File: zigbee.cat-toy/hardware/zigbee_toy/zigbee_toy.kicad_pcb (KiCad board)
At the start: 2 copper layers, 40 x 26 mm, 60 parts, among them J1 USB-C 16P, J2 SWD, J3 LiPo 1S (JST-PH), J4 MOTOR, J5 SPEAKER, Q1 AO3401A, Q2 AO3400A, SW1 PAIR, U1 E73-2G4M08S1C, U2 DRV8213DSGR, U3 LIS2DH12TR, U4 TP4054-42-SOT25R, U5 XB5353A, Y1 32.768k 12.5pF

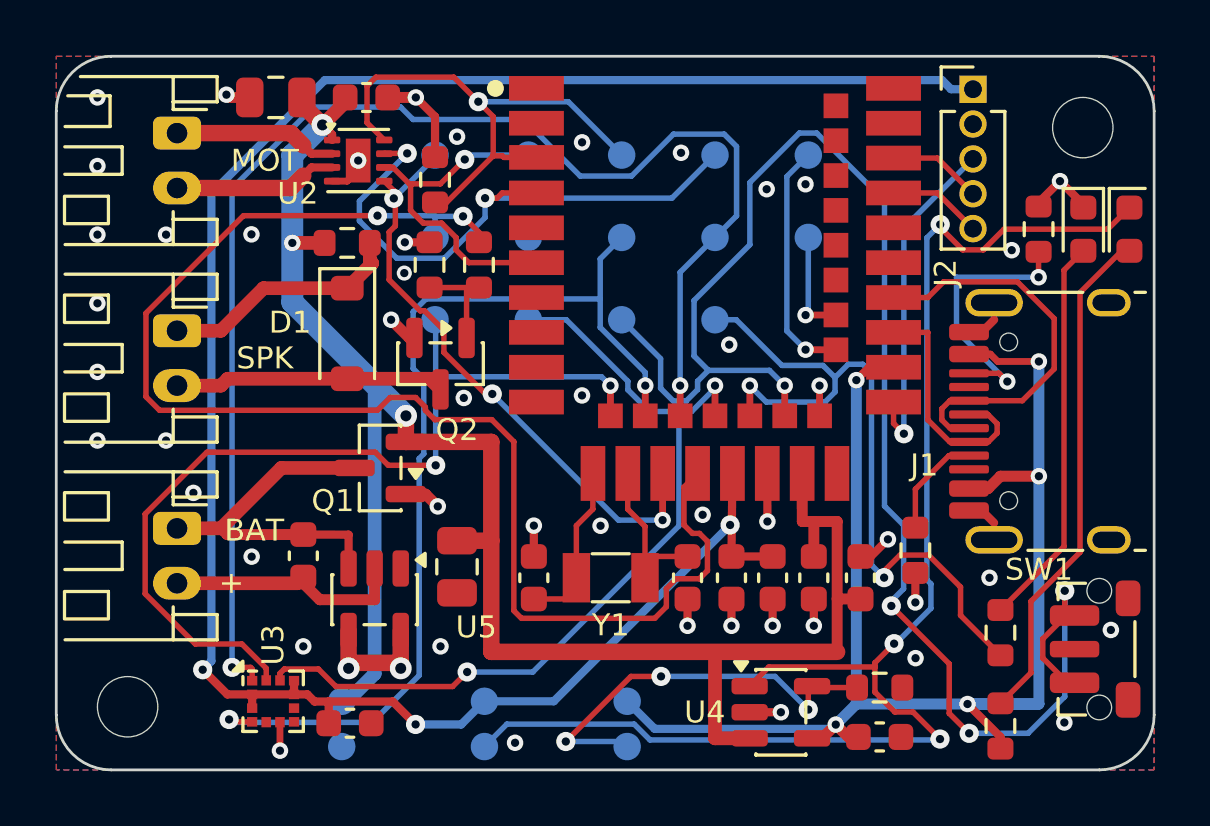
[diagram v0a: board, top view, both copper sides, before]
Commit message: zigbee.cat-toy: rev B board (ESP32-C6), JLC Economic PCBA
- ESP32-C6-MINI-1U-H4 replaces the nRF52840 E73; RT9080 3.3 V regulator,
  1M/1M battery divider, MSKSEMI LIS2DW12TR-MS accelerometer (not ST's),
  one red status LED. Every assembled part is Economic-eligible.
- Module 1 mm from the top edge (JLC Economic edge rule); antenna keepout
  so the PCB-antenna MINI-1 drops onto the same pads.
- Re-routed: USB pair under the module edge, nothing on F.Cu under the
  USB-C, no B.Cu under the crystal, 10 uF at the module 3V3 pin.
- Ball and pod checks cover a MINI-1 antenna overhang.
- README rewritten for rev B; rev A lives under the zigbee.cat-toy/rev-a tag.

Co-Authored-By: Claude Opus 5.5 <noreply@anthropic.com>
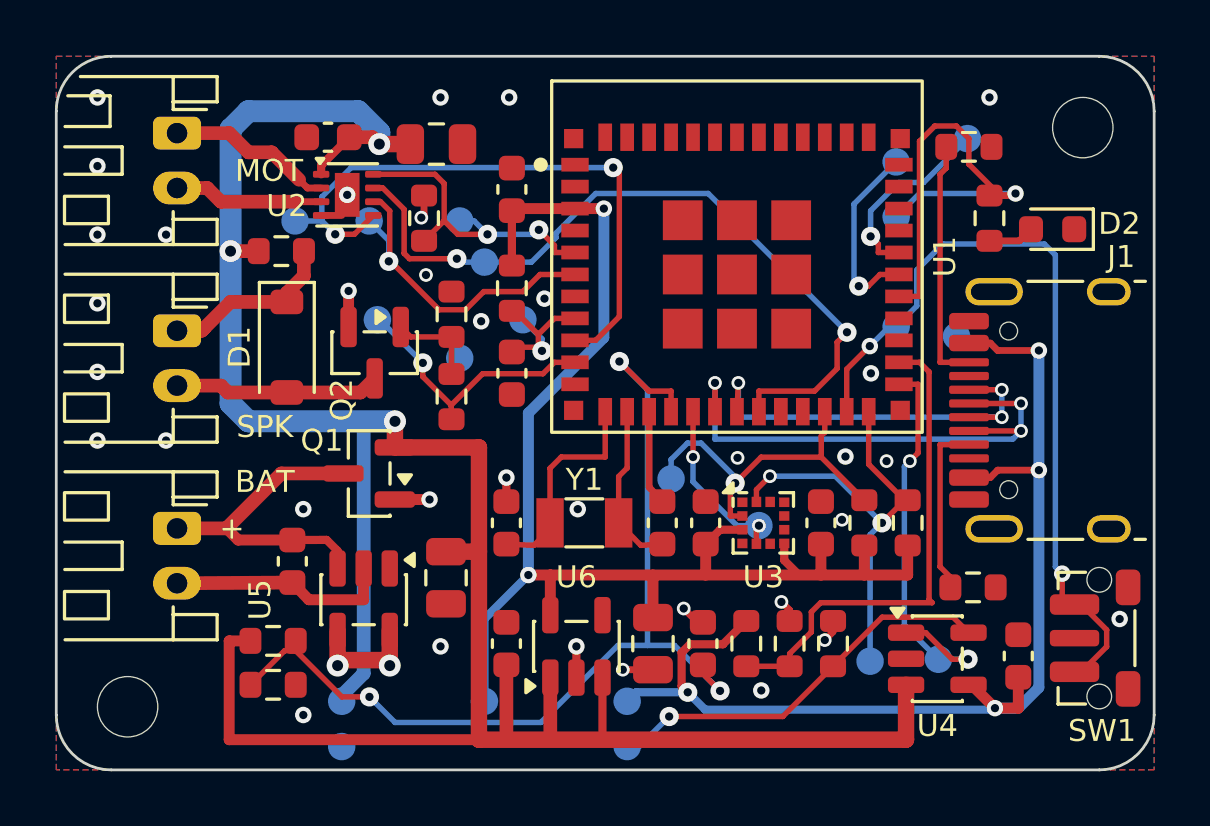
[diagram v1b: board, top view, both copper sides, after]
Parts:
- removed C7: 100n, Capacitor_SMD:C_0603_1608Metric
- removed D3: RED (status), LED_SMD:LED_0603_1608Metric
- removed J2: SWD, Connector_PinHeader_1.27mm:PinHeader_1x05_P1.27mm_Vertical
- removed R5: 1k, Resistor_SMD:R_0603_1608Metric
- removed TP14: INT2, TestPoint:TestPoint_Pad_D1.0mm
- added C11: 100n, Capacitor_SMD:C_0603_1608Metric, F.Cu at (23.7, 17.0)
- added C16: 100n, Capacitor_SMD:C_0603_1608Metric, F.Cu at (23.6, 21.4)
- added C5: 1u, Capacitor_SMD:C_0603_1608Metric, F.Cu at (16.6, 11.6)
- added R12: 1M, Resistor_SMD:R_0603_1608Metric, F.Cu at (7.90, 21.3)
- added R13: 1M, Resistor_SMD:R_0603_1608Metric, F.Cu at (7.90, 22.9)
- added R14: 68k, Resistor_SMD:R_0603_1608Metric, F.Cu at (25.1, 21.4)
- added R15: 100k, Resistor_SMD:R_0603_1608Metric, F.Cu at (26.7, 21.4)
- added R16: 4.7k, Resistor_SMD:R_0603_1608Metric, F.Cu at (29.4, 17.0)
- added R17: 4.7k, Resistor_SMD:R_0603_1608Metric, F.Cu at (31.0, 17.0)
- added R9: 10k, Resistor_SMD:R_0603_1608Metric, F.Cu at (16.6, 8.45)
- added TP21: EN, TestPoint:TestPoint_Pad_D1.0mm, B.Cu at (17.0, 9.60)
- added TP22: GND, TestPoint:TestPoint_Pad_D1.0mm, B.Cu at (32.8, 10.2)
- added U6: RT9080-33GJ5, Package_TO_SOT_SMD:TSOT-23-5, F.Cu at (18.9, 21.5)
- C8: value 4.7u -> 22u; footprint Capacitor_SMD:C_0603_1608Metric -> Capacitor_SMD:C_0805_2012Metric
- C9: value 100n -> 10u
- D2: value RED (charging) -> RED (status)
- SW1: value PAIR -> PAIR / BOOT
- TP17: value BTN -> BOOT
- TP2: value VDD -> 3V3
- U1: value E73-2G4M08S1C -> ESP32-C6-MINI-1U-H4; footprint zigbee_toy:Ebyte_E73-2G4M08S1C -> zigbee_toy:ESP32-C6-MINI-1U
- U3: value LIS2DH12TR -> LIS2DW12TR-MS
- moved U3 19.0 mm to (25.8, 17.0)
- moved C10 18.6 mm to (27.9, 17.0), turned to 90 degrees
- moved R4 18.5 mm to (34.0, 5.90), turned to -90 degrees
- moved TP5 16.8 mm to (32.1, 22.0)
- moved TP16 16.4 mm to (29.6, 22.0)
- moved C9 16.3 mm to (16.6, 4.85), turned to 90 degrees
- moved TP13 14.0 mm to (25.6, 17.1)
- moved C6 13.1 mm to (16.4, 21.4)
- moved TP17 10.0 mm to (30.6, 9.85)
- moved TP10 9.26 mm to (15.6, 7.50)
- moved TP15 8.98 mm to (22.4, 15.4)
- moved TP18 7.59 mm to (30.6, 5.85)
- moved TP9 6.37 mm to (14.7, 6.00)
- moved TP8 6.28 mm to (11.4, 6.00)
- moved C2 6.09 mm to (13.8, 3.20), turned to 0 degrees
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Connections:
- net XL2 renamed XTAL_N
- C10 pad 1: VDD -> 3V3
- C12 pad 1: XL1 -> XTAL_P
- C8 pad 1: VDD -> 3V3
- C9 pad 1: VDD -> 3V3
- D2 pad 1: CHG_STAT -> GND
- D2 pad 2: CHG_LED -> LED_A
- R4 pad 1: VBUS -> LED_STATUS
- R4 pad 2: CHG_LED -> LED_A
- TP2 pad 1: VDD -> 3V3
- U1 pad 1: (no net) -> GND
- U1 pad 10: (no net) -> SPK_PWM
- U1 pad 11: XL1 -> GND
- U1 pad 12: ACC_INT1 -> XTAL_P
- U1 pad 14: I2C_SDA -> GND
- U1 pad 15: MOT_PWM -> VBAT_SENSE
- U1 pad 16: I2C_SCL -> ACC_INT1
- U1 pad 17: SPK_PWM -> USB_DN
- U1 pad 18: ACC_INT2 -> USB_DP
- U1 pad 19: VDD -> MOT_GAINSEL
- U1 pad 2: (no net) -> GND
- U1 pad 20: LED_STATUS -> (no net)
- U1 pad 21: GND -> (no net)
- U1 pad 22: BTN -> I2C_SDA
- U1 pad 23: VBAT -> BTN
- U1 pad 24: GND -> I2C_SCL
- U1 pad 25: (no net) -> CHG_STAT
- U1 pad 26: nRESET -> VBUS_SENSE
- U1 pad 27: VBUS -> (no net)
- U1 pad 28: DBG_TX -> (no net)
- U1 pad 29: USB_DN -> LED_STATUS
- U1 pad 3: MOT_IPROPI -> 3V3
- U1 pad 31: USB_DP -> DBG_TX
- U1 pad 36: (no net) -> GND
- U1 pad 37: SWDIO -> GND
- U1 pad 38: (no net) -> GND
- U1 pad 39: SWCLK -> GND
- U1 pad 4: MOT_GAINSEL -> (no net)
- U1 pad 40: (no net) -> GND
- U1 pad 41: (no net) -> GND
- U1 pad 42: (no net) -> GND
- U1 pad 43: (no net) -> GND
- U1 pad 5: GND -> MOT_IPROPI
- U1 pad 8: (no net) -> EN
- U1 pad 9: (no net) -> MOT_PWM
- U3 pad 1: I2C_SCL -> (no net)
- U3 pad 10: VDD -> (no net)
- U3 pad 11: ACC_INT2 -> (no net)
- U3 pad 12: ACC_INT1 -> I2C_SCL
- U3 pad 2: VDD -> I2C_SDA
- U3 pad 3: VDD -> 3V3
- U3 pad 4: I2C_SDA -> (no net)
- U3 pad 5: GND -> ACC_INT1
- U3 pad 6: GND -> (no net)
- U3 pad 7: GND -> 3V3
- U3 pad 9: VDD -> GND
- Y1 pad 1: XL1 -> XTAL_P
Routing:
- net VDD: track 76.6 -> 0.00 mm, vias 3 -> 0
- net 3V3: track 0.00 -> 49.3 mm, vias 0 -> 2
- net SPK_PWM: track 51.2 -> 9.95 mm, vias 2 -> 1
- net CHG_STAT: track 51.3 -> 15.2 mm, vias 3 -> 2
- net VBAT_SENSE: track 0.00 -> 36.0 mm, vias 0 -> 3
- net I2C_SCL: track 50.8 -> 16.2 mm
- net ACC_INT2: track 31.6 -> 0.00 mm, vias 2 -> 0
- net BTN: track 57.9 -> 29.0 mm, vias 4 -> 2
- net ACC_INT1: track 33.5 -> 6.31 mm
- net I2C_SDA: track 36.5 -> 13.2 mm, vias 2 -> 1
- net VBAT: track 69.3 -> 92.5 mm
- net CHG_LED: track 18.6 -> 0.00 mm
- net VBUS_SENSE: track 0.00 -> 18.1 mm
- net GND: track 30.6 -> 17.3 mm, vias 50 -> 37
- net LED_A: track 14.3 -> 1.69 mm
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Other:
- board text added: "3V3"
- board text added: "BOOT"
- board text added: "EN"
- board text added: "rev B 2026-10"
- board text removed: "CHG"
- board text removed: "CLK"
- board text removed: "DIO"
- board text removed: "INT2"
- board text removed: "RST"
- board text removed: "VDD"
- board text removed: "rev A 2026-10"

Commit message: zigbee.cat-toy: rev B review fixes (driver ground loop, module vias, silk)
From an EE friend's review and the DRV8213 datasheet's layout section:
- C3 flipped so its ground pad drops straight onto the driver's thermal
  pad (return path 14.7 mm -> 1.2 mm); two thermal pad vias instead of one;
  ground via at C2 (18.7 mm -> 4.1 mm)
- IN2 rerouted on the back layer below the driver instead of under it, so
  the back plane under the driver is whole again; EN reshuffled to make room,
  TP21 sits on the EN via
- C2 10 uF -> 22 uF (same part as C1/C8)
- vias in 7 of the module's 9 centre ground pads (module ground to the
  driver 21 mm -> 6.5 mm)
- route generator chamfers 90-degree corners (29 -> 8, the rest inside pads
  or on vias)
- front refs all horizontal, one size; title and paw moved into the bare
  antenna keepout strip on the back
- MOT_DIR/MOT_PWM renamed MOT_IN1/MOT_IN2: PWM drive/brake on both pins
  (drive/coast loses IPROPI while coasting)

Co-Authored-By: Claude Opus 5.5 <noreply@anthropic.com>
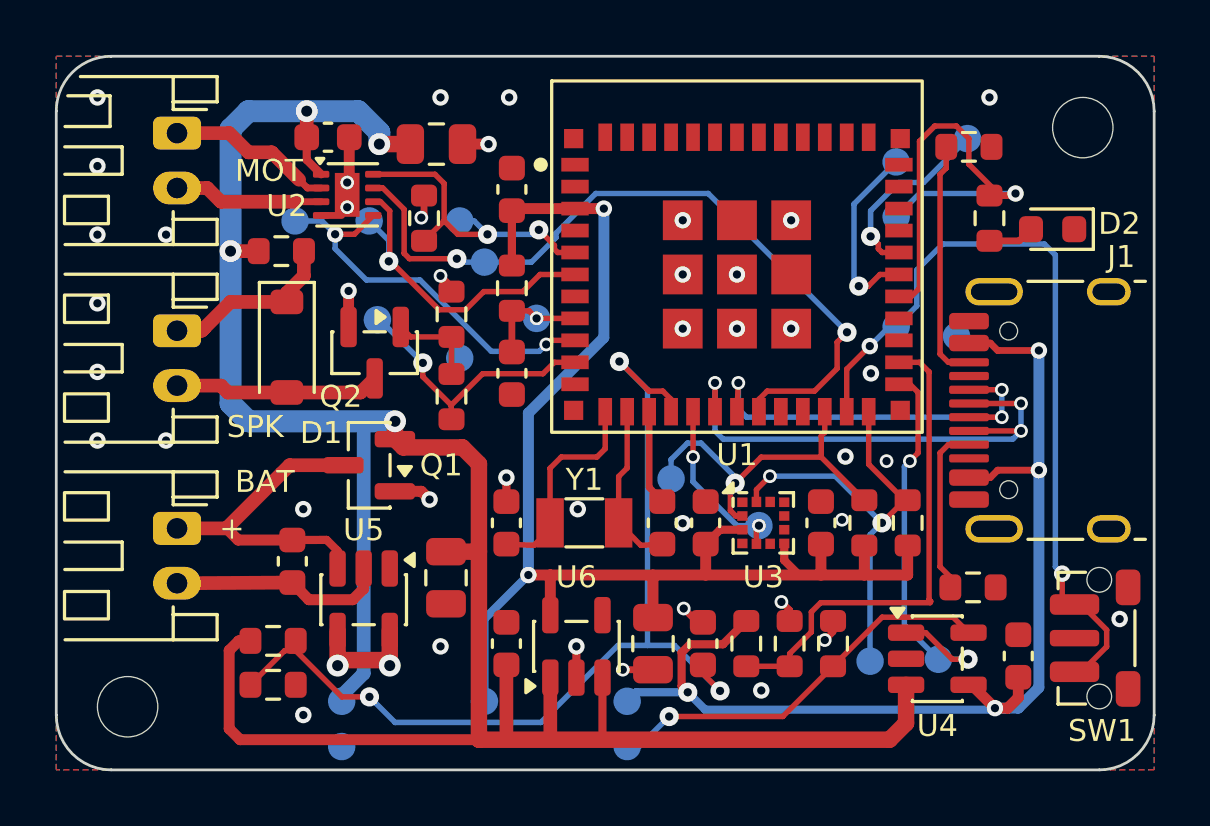
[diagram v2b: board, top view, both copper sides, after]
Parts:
- C2: value 10u 25V -> 22u
- TP7: value PWM -> IN2
- TP8: value DIR -> IN1
- moved TP21 0.50 mm to (17.5, 9.55)
- moved Q1 0.30 mm to (11.4, 14.9)
- turned C3 to 0 degrees
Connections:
- net MOT_DIR renamed MOT_IN1
- net MOT_PWM renamed MOT_IN2
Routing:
- net MOT_IN2: track 22.8 -> 14.3 mm
- net GND: track 17.3 -> 20.6 mm, vias 37 -> 44
- net EN: track 6.01 -> 3.91 mm
- net VBAT: track 92.5 -> 90.7 mm, vias 3 -> 4
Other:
- board text added: "IN1"
- board text added: "IN2"
- board text removed: "DIR"
- board text removed: "PWM"

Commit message: zigbee.cat-toy: rev B shrunk to 36 x 23 mm (was 40 x 26)
- 0402 Basic passives; bulk caps stay 0603/0805. VBUS divider 33k/51k
  (68k has no Basic 0402)
- motor and speaker on JST-SH (SMD, assembled); battery stays JST-PH
- USBLC6-2SC6 on D+/D-; 10 nF on IPROPI (DRV8213 datasheet 8.4.2.2)
- new floorplan and routing: power, driver loop, USB, BTN, the
  accelerometer block and ground vias by hand, the rest Freerouting
  (frozen); every ground pad has its own via or reaches the pour
- module pins 25/26 swapped: VBUS_SENSE on IO19, CHG_STAT on IO20
- the button's two pin-1 pads count as one terminal (KiCad jumper pads)
- gen_silk clips footprint outlines at pads and other parts' silk;
  check_spacing.py checks real body/pad gaps, courtyard overlap is a
  warning
- pod.py and ball.py read the board from placement.py; pod bay grows for
  the 103450 cell; ball board moves so the H2 standoff clears the motor.
  Both --check CLEAN against the new board STEP

Co-Authored-By: Claude Opus 5.5 <noreply@anthropic.com>
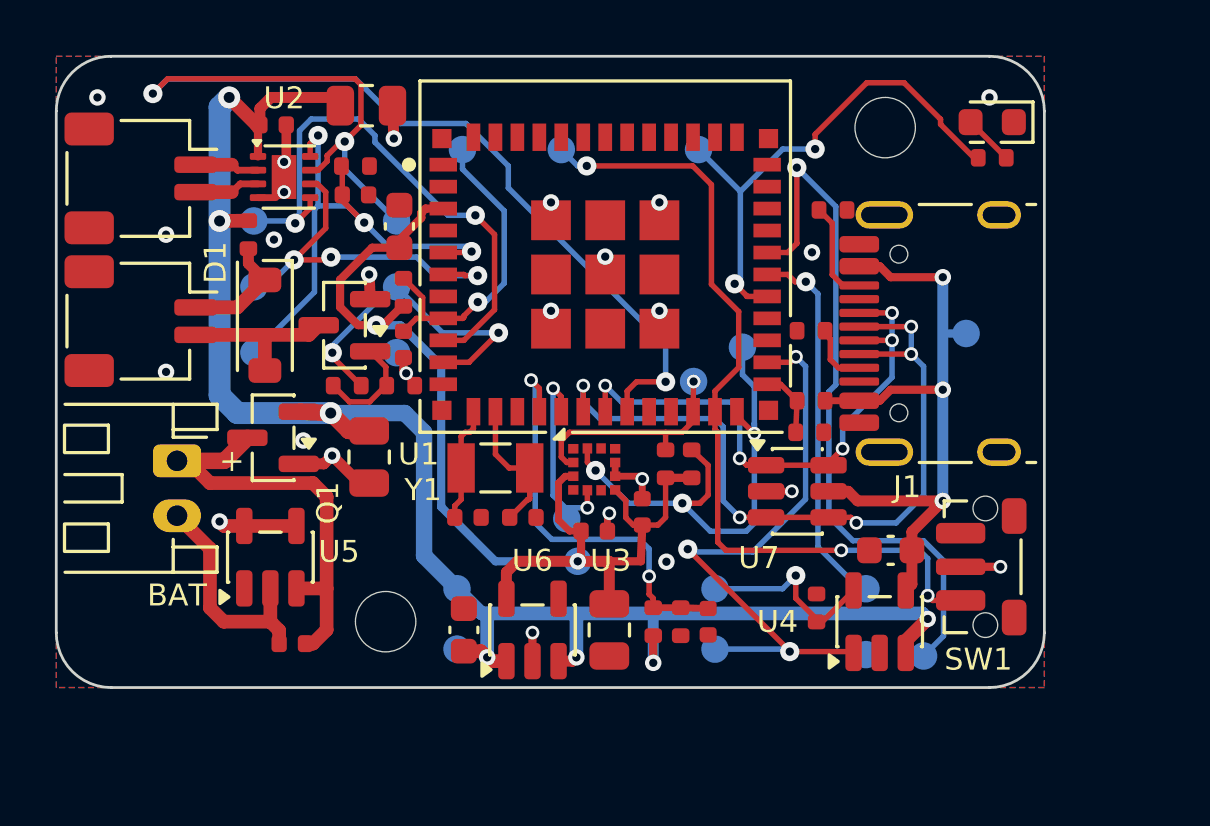
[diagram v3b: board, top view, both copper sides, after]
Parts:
- added C7: 10n, Capacitor_SMD:C_0402_1005Metric, F.Cu at (10.9, 5.05)
- added U7: USBLC6-2SC6, Package_TO_SOT_SMD:SOT-23-6, F.Cu at (27.0, 15.8)
- C10, C11, C12, C13, C15, C16, C3, C5: footprint Capacitor_SMD:C_0603_1608Metric -> Capacitor_SMD:C_0402_1005Metric
- J4, J5: footprint Connector_JST:JST_PH_S2B-PH-K_1x02_P2.00mm_Horizontal -> Connector_JST:JST_SH_SM02B-SRSS-TB_1x02-1MP_P1.00mm_Horizontal
- R1, R11, R12, R13, R16, R17, R2, R3, R4, R6, R7, R8, R9: footprint Resistor_SMD:R_0603_1608Metric -> Resistor_SMD:R_0402_1005Metric
- R14: value 68k -> 33k; footprint Resistor_SMD:R_0603_1608Metric -> Resistor_SMD:R_0402_1005Metric
- R15: value 100k -> 51k; footprint Resistor_SMD:R_0603_1608Metric -> Resistor_SMD:R_0402_1005Metric
- moved TP19 18.9 mm to (31.6, 21.9)
- moved TP3 18.2 mm to (33.1, 10.1)
- moved TP20 15.6 mm to (29.5, 19.4)
- moved R13 15.0 mm to (22.8, 20.6), turned to -90 degrees
- moved R12 13.9 mm to (21.8, 20.6), turned to 90 degrees
- moved TP17 13.8 mm to (18.4, 3.40)
- moved TP16 12.3 mm to (25.0, 10.6)
- moved TP22 12.1 mm to (29.5, 21.8)
- moved R1 11.1 mm to (27.5, 10.0), turned to 180 degrees
- moved H2 9.90 mm to (12.0, 20.6)
- moved R14 9.16 mm to (27.5, 12.6), turned to 180 degrees
- moved TP9 8.90 mm to (7.20, 10.8)
- moved R17 8.16 mm to (23.1, 14.8)
- moved TP5 8.15 mm to (24.0, 21.6)
- moved R15 7.73 mm to (27.4, 13.7), turned to 0 degrees
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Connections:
- U1 pad 25: CHG_STAT -> VBUS_SENSE
- U1 pad 26: VBUS_SENSE -> CHG_STAT
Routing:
- net VBAT: track 90.7 -> 63.3 mm, vias 4 -> 7
- net VBAT_SENSE: track 35.8 -> 15.3 mm, vias 3 -> 2
- net DBG_TX: track 6.93 -> 26.0 mm
- net VBUS: track 41.2 -> 24.8 mm, vias 4 -> 3
- net VBUS_SENSE: track 18.0 -> 2.49 mm
- net MOT_GAINSEL: track 27.8 -> 42.7 mm, vias 2 -> 3
- net USB_DN: track 19.0 -> 27.9 mm, vias 3 -> 5
- net 3V3: track 49.3 -> 41.5 mm
- net EN: track 3.91 -> 11.7 mm
- net MOT_IPROPI: track 11.8 -> 19.5 mm, vias 2 -> 3
- net CHG_PROG: track 14.6 -> 7.10 mm
- net CHG_STAT: track 15.0 -> 22.0 mm, vias 2 -> 3
- net DBG_RX: track 6.87 -> 13.7 mm
- net MOT_IN2: track 14.3 -> 20.3 mm
- net CC2: track 8.82 -> 3.70 mm
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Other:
- board size 40 x 26 mm -> 36 x 23 mm
- board text added: "2026-10"
- board text added: "rev B"
- board text removed: "MOT"
- board text removed: "rev B 2026-10"

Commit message: zigbee.cat-toy: fixes from the rev B datasheet review
docs/design_review_rev_b.md (Fable) found three must-fix issues:
- USBLC6 pin 5 moves from VBUS to 3V3: the C6 enables its D+ pull-up
  from boot, which back-fed VBUS through the steering diode while
  unplugged (~1.7 V on VBUS_SENSE, ~75 uA leak through the divider and
  the TP4054). U7 rotated so pin 5 faces the module side; BTN rerouted on
  the back along the top and down the right edge to free that corridor
- R10 10k pull-up on CHG_STAT: the TP4054's charge-done state is a
  20 uA pull-down, which beats the C6's internal ~45k pull-up
- charge current is 260 mA with R3 = 3.3k (1000/I only holds to
  150 mA); docs corrected, R3 kept (cooler charger)

README: firmware notes from the review (low-battery cutoff, charge-state
decode, driver auto-sleep, 324 mA default for the JST-SH motor lead,
charger heat) and the review's should-fix items listed as open.
DRC clean, spacing ok, JLC export 47 parts, pod/ball --check CLEAN.

Co-Authored-By: Claude Opus 5.5 <noreply@anthropic.com>
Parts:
- added R10: 10k, Resistor_SMD:R_0402_1005Metric, F.Cu at (23.9, 17.5)
- turned U7 to 180 degrees
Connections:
- U7 pad 1: USB_DP -> USB_DN
- U7 pad 3: USB_DN -> USB_DP
- U7 pad 4: USB_DN -> USB_DP
- U7 pad 5: VBUS -> 3V3
- U7 pad 6: USB_DP -> USB_DN
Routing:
- net BTN: track 30.4 -> 49.2 mm, vias 3 -> 2
- net VBUS: track 24.8 -> 20.5 mm
- net 3V3: track 41.5 -> 45.7 mm
- net GND: track 16.9 -> 15.9 mm, vias 25 -> 24
- net CHG_STAT: track 22.0 -> 22.9 mm
